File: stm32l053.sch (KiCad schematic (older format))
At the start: 17 parts, among them P1 SWD, P2 CONN_01X23, P3 CONN_01X23, P4 BOOT0, P5 Ext Xtal, SW1 SW_PUSH, U1 STM32_LQFP64

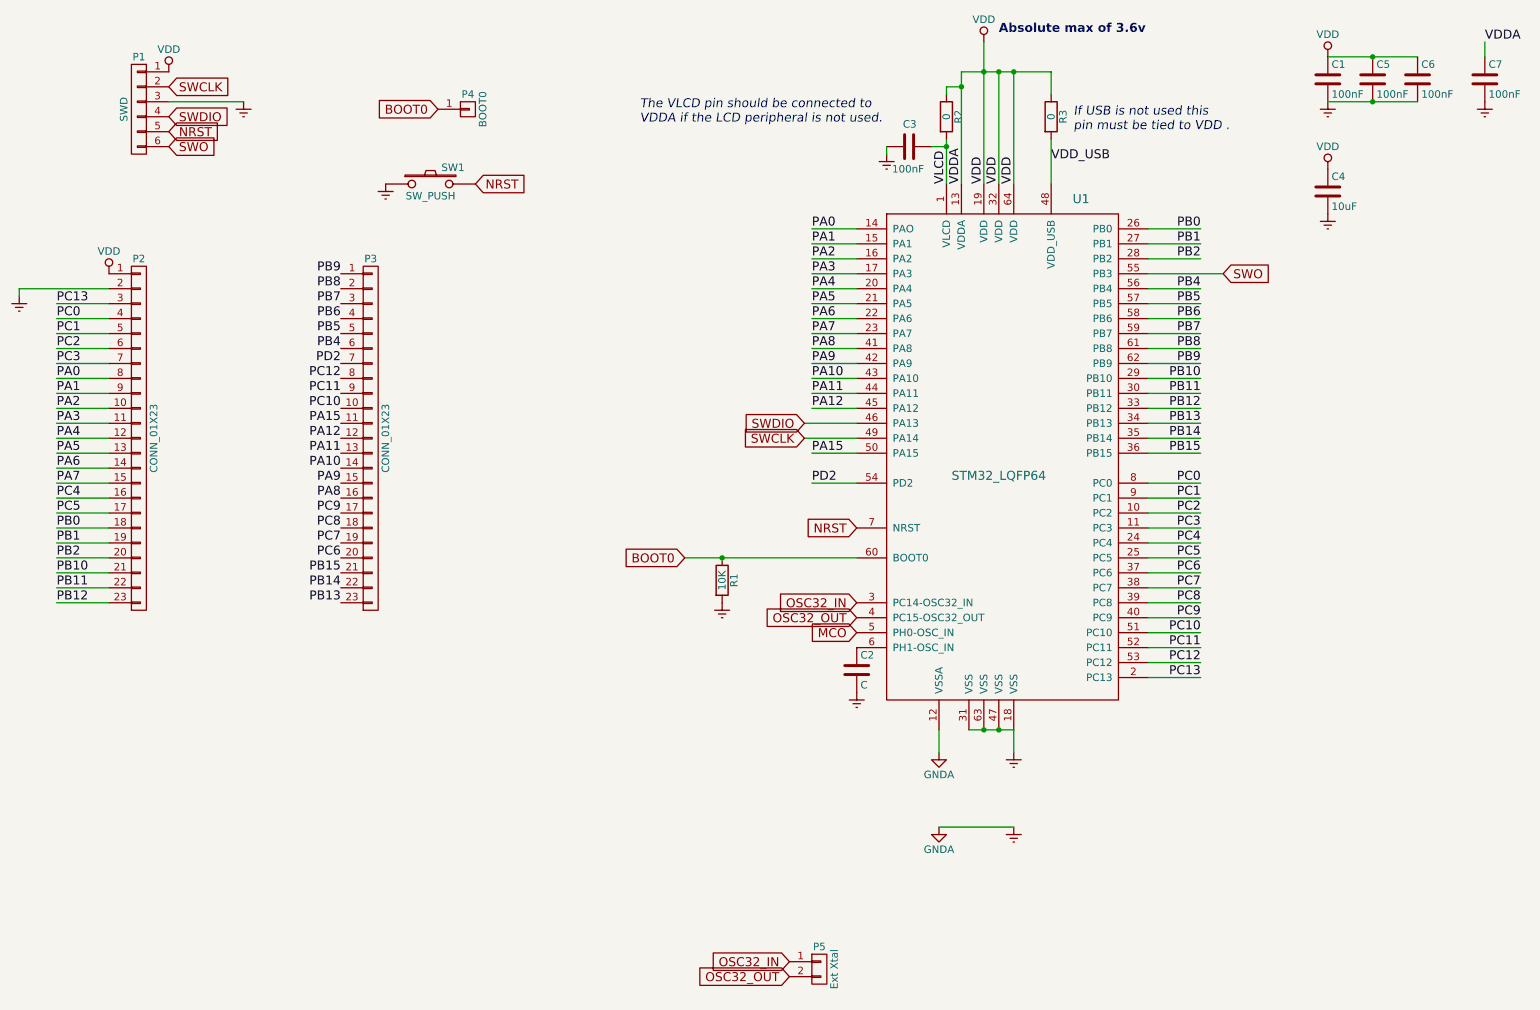
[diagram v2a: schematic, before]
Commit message: GPIO initial routing
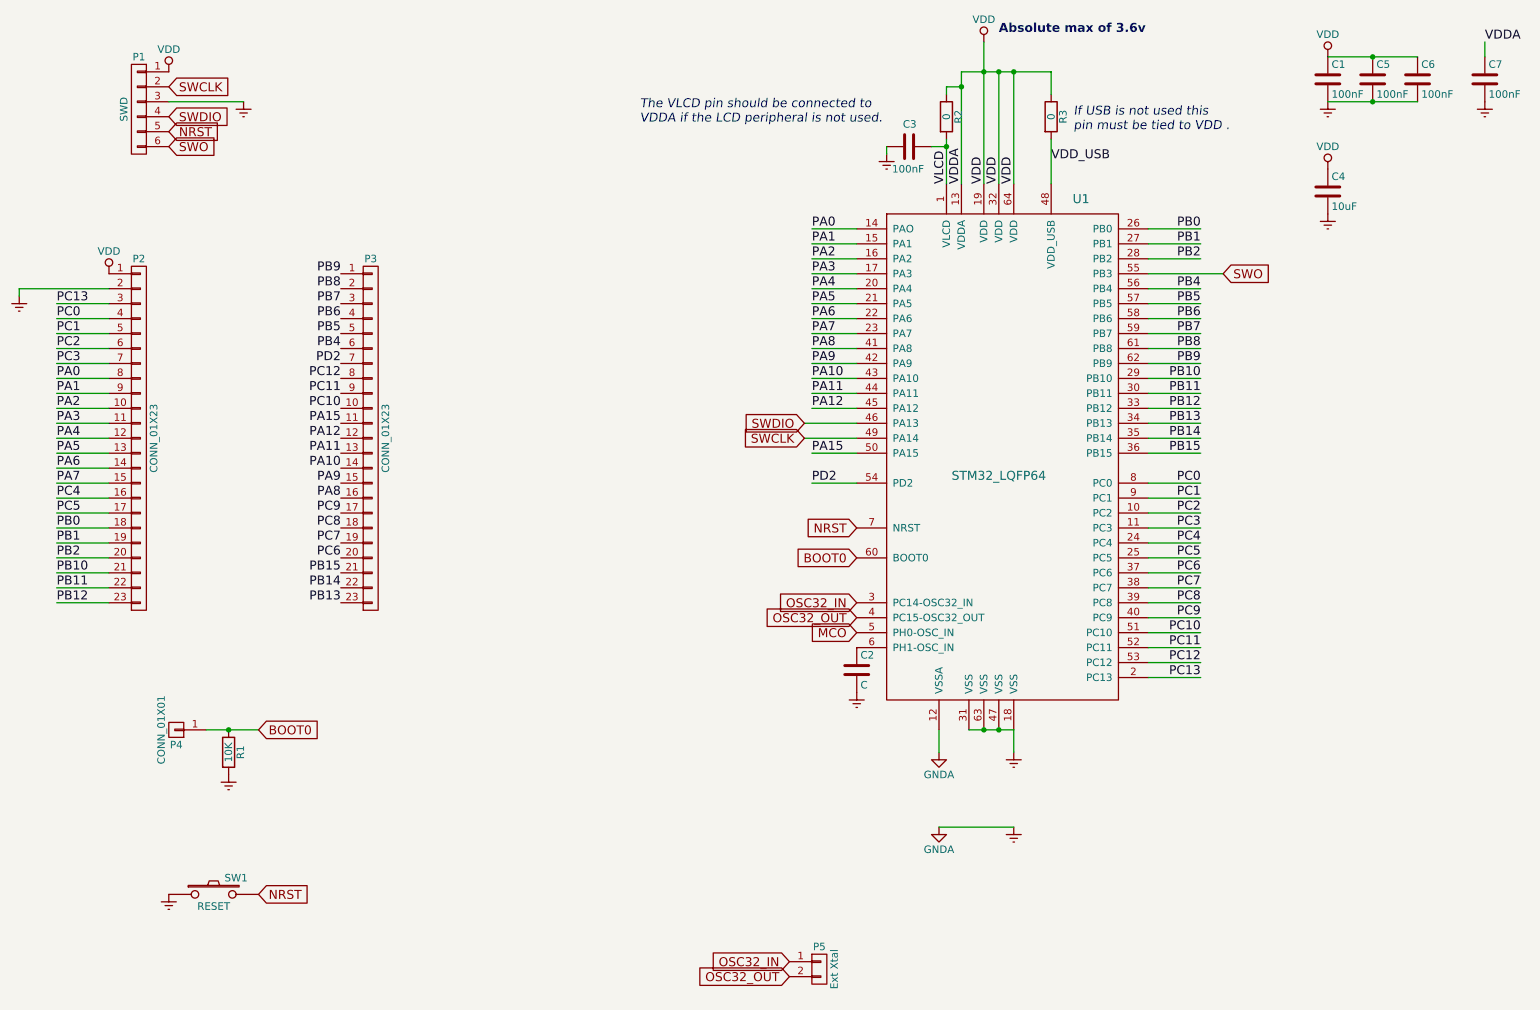
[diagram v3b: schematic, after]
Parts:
- P4: value BOOT0 -> CONN_01X01; footprint Pin_Headers:Pin_Header_Straight_1x01 -> Measurement_Points:Measurement_Point_Round-SMD-Pad_Small
- SW1: value SW_PUSH -> RESET; footprint Buttons_Switches_SMD:SW_SPST_B3U-1000P -> Buttons_Switches_ThroughHole:SW_PUSH_6mm
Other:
- moved on the sheet: R1, SW1
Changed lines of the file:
@@
 L Earth #PWR08
 U 1 1 5802320E
-P 5600 4700
-F 0 "#PWR08" H 5600 4450 50  0001 C CNN
-F 1 "Earth" H 5600 4550 50  0001 C CNN
-F 2 "" H 5600 4700 50  0000 C CNN
-F 3 "" H 5600 4700 50  0000 C CNN
-	1    5600 4700
+P 2300 5850
+F 0 "#PWR08" H 2300 5600 50  0001 C CNN
+F 1 "Earth" H 2300 5700 50  0001 C CNN
+F 2 "" H 2300 5850 50  0000 C CNN
+F 3 "" H 2300 5850 50  0000 C CNN
+	1    2300 5850
 	1    0    0    -1
 $EndComp
@@
 L R R1
 U 1 1 58037533
-P 5600 4550
-F 0 "R1" V 5680 4550 50  0000 C CNN
-F 1 "10K" V 5600 4550 50  0000 C CNN
-F 2 "Resistors_SMD:R_0805_HandSoldering" V 5530 4550 50  0001 C CNN
-F 3 "" H 5600 4550 50  0000 C CNN
-	1    5600 4550
-	1    0    0    -1
-$EndComp
-Text GLabel 5350 4400 0    60   Input ~ 0
+P 2300 5700
+F 0 "R1" V 2380 5700 50  0000 C CNN
+F 1 "10K" V 2300 5700 50  0000 C CNN
+F 2 "Resistors_SMD:R_0805_HandSoldering" V 2230 5700 50  0001 C CNN
+F 3 "" H 2300 5700 50  0000 C CNN
+	1    2300 5700
+	1    0    0    -1
+$EndComp
+Text GLabel 6500 4400 0    60   Input ~ 0
 BOOT0
 Text GLabel 6500 4700 0    60   Input ~ 0
@@
 Text Label 3050 4500 2    60   ~ 0
 PB15
-Wire Wire Line
-	5350 4400 6500 4400
-Connection ~ 5600 4400
 Text Label 8800 3900 2    60   ~ 0
 PC0
@@
 	1    0    0    -1
 $EndComp
-Text GLabel 3700 1400 0    60   Input ~ 0
+Text GLabel 2500 5550 2    60   Input ~ 0
 BOOT0
 $Comp
 L SW_PUSH SW1
 U 1 1 5803EFB1
-P 3650 1900
-F 0 "SW1" H 3800 2010 50  0000 C CNN
-F 1 "SW_PUSH" H 3650 1820 50  0000 C CNN
-F 2 "Buttons_Switches_SMD:SW_SPST_B3U-1000P" H 3650 1900 50  0001 C CNN
-F 3 "" H 3650 1900 50  0000 C CNN
-	1    3650 1900
+P 2200 6650
+F 0 "SW1" H 2350 6760 50  0000 C CNN
+F 1 "RESET" H 2200 6570 50  0000 C CNN
+F 2 "Buttons_Switches_ThroughHole:SW_PUSH_6mm" H 2200 6650 50  0001 C CNN
+F 3 "" H 2200 6650 50  0000 C CNN
+	1    2200 6650
 	1    0    0    -1
 $EndComp
@@
 L Earth #PWR014
 U 1 1 5803F003
-P 3350 1900
-F 0 "#PWR014" H 3350 1650 50  0001 C CNN
-F 1 "Earth" H 3350 1750 50  0001 C CNN
-F 2 "" H 3350 1900 50  0000 C CNN
-F 3 "" H 3350 1900 50  0000 C CNN
-	1    3350 1900
-	1    0    0    -1
-$EndComp
-Text GLabel 3950 1900 2    60   Input ~ 0
+P 1900 6650
+F 0 "#PWR014" H 1900 6400 50  0001 C CNN
+F 1 "Earth" H 1900 6500 50  0001 C CNN
+F 2 "" H 1900 6650 50  0000 C CNN
+F 3 "" H 1900 6650 50  0000 C CNN
+	1    1900 6650
+	1    0    0    -1
+$EndComp
+Text GLabel 2500 6650 2    60   Input ~ 0
 NRST
 $Comp
@@
 F 3 "" H 9650 1950 50  0000 C CNN
 	1    9650 1950
-	1    0    0    -1
-$EndComp
-$Comp
-L CONN_01X01 P4
-U 1 1 5803B76E
-P 3900 1400
-F 0 "P4" H 3900 1500 50  0000 C CNN
-F 1 "BOOT0" V 4000 1400 50  0000 C CNN
-F 2 "Pin_Headers:Pin_Header_Straight_1x01" H 3900 1400 50  0001 C CNN
-F 3 "" H 3900 1400 50  0000 C CNN
-	1    3900 1400
 	1    0    0    -1
 $EndComp
@@
 Connection ~ 7450 1150
 Connection ~ 7550 1150
+$Comp
+L CONN_01X01 P4
+U 1 1 580498F7
+P 1950 5550
+F 0 "P4" H 1950 5650 50  0000 C CNN
+F 1 "CONN_01X01" V 2050 5550 50  0000 C CNN
+F 2 "Measurement_Points:Measurement_Point_Round-SMD-Pad_Small" H 1950 5550 50  0001 C CNN
+F 3 "" H 1950 5550 50  0000 C CNN
+	1    1950 5550
+	-1   0    0    1
+$EndComp
+Wire Wire Line
+	2150 5550 2500 5550
+Connection ~ 2300 5550
 $EndSCHEMATC

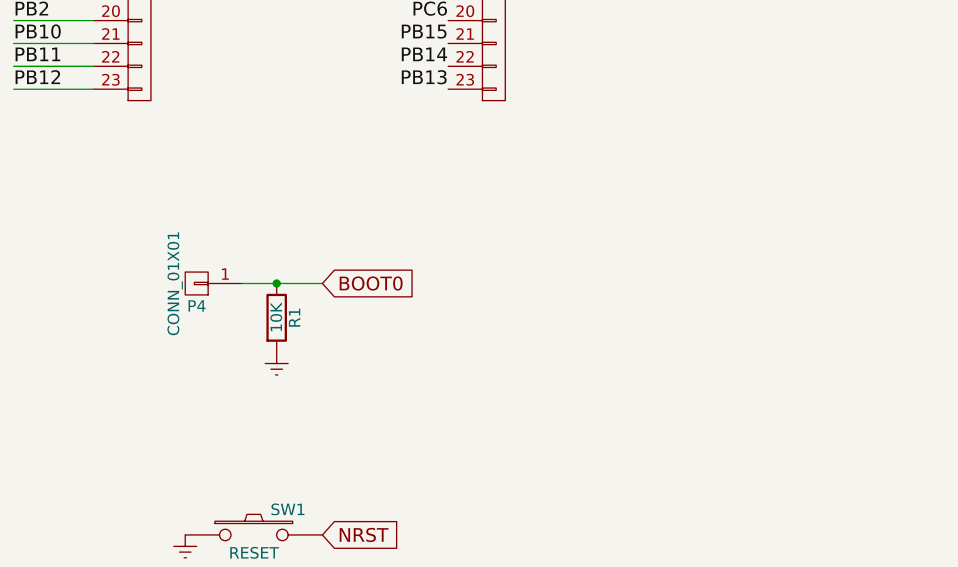
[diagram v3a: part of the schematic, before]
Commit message: SWO header
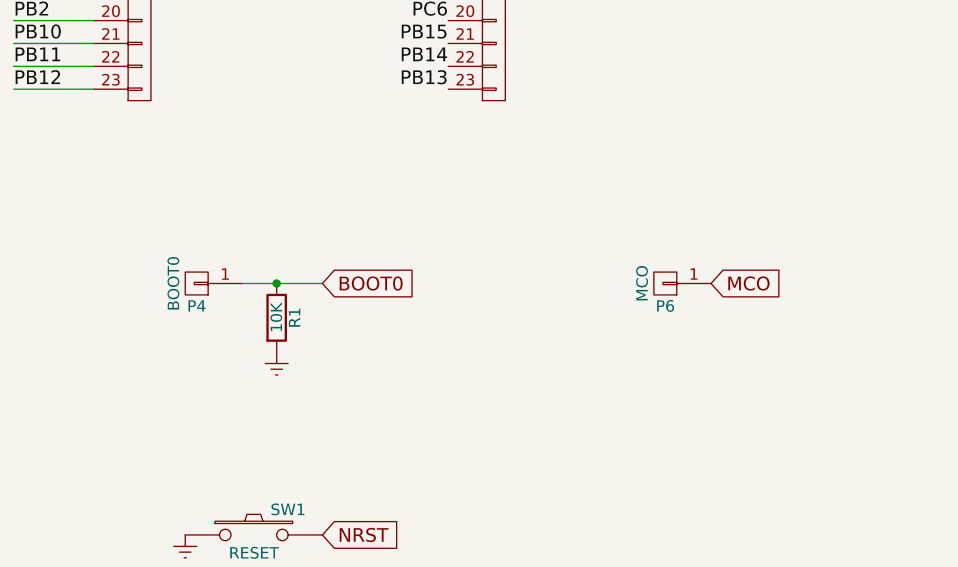
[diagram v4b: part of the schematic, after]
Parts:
- added P6: MCO, Measurement_Points:Measurement_Point_Round-SMD-Pad_Small, symbol CONN_01X01
- P4: value CONN_01X01 -> BOOT0
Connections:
- net MCO: now also P6.1 (P1)
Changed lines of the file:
@@
 $EndComp
 $Comp
-L Earth #PWR01
+L Earth #PWR15
 U 1 1 58021BE1
 P 9650 1350
-F 0 "#PWR01" H 9650 1100 50  0001 C CNN
+F 0 "#PWR15" H 9650 1100 50  0001 C CNN
 F 1 "Earth" H 9650 1200 50  0001 C CNN
 F 2 "" H 9650 1350 50  0000 C CNN
@@
 $EndComp
 $Comp
-L VDD #PWR02
+L VDD #PWR14
 U 1 1 58021C2A
 P 9650 1050
-F 0 "#PWR02" H 9650 900 50  0001 C CNN
+F 0 "#PWR14" H 9650 900 50  0001 C CNN
 F 1 "VDD" H 9650 1200 50  0000 C CNN
 F 2 "" H 9650 1050 50  0000 C CNN
@@
 $EndComp
 $Comp
-L GNDA #PWR03
+L GNDA #PWR10
 U 1 1 58021F75
 P 7050 6200
-F 0 "#PWR03" H 7050 5950 50  0001 C CNN
+F 0 "#PWR10" H 7050 5950 50  0001 C CNN
 F 1 "GNDA" H 7050 6050 50  0000 C CNN
 F 2 "" H 7050 6200 50  0000 C CNN
@@
 $EndComp
 $Comp
-L Earth #PWR04
+L Earth #PWR13
 U 1 1 58021F89
 P 7550 6200
-F 0 "#PWR04" H 7550 5950 50  0001 C CNN
+F 0 "#PWR13" H 7550 5950 50  0001 C CNN
 F 1 "Earth" H 7550 6050 50  0001 C CNN
 F 2 "" H 7550 6200 50  0000 C CNN
@@
 $EndComp
 $Comp
-L GNDA #PWR05
+L GNDA #PWR9
 U 1 1 58022154
 P 7050 5700
-F 0 "#PWR05" H 7050 5450 50  0001 C CNN
+F 0 "#PWR9" H 7050 5450 50  0001 C CNN
 F 1 "GNDA" H 7050 5550 50  0000 C CNN
 F 2 "" H 7050 5700 50  0000 C CNN
@@
 $EndComp
 $Comp
-L Earth #PWR06
+L Earth #PWR12
 U 1 1 580221FA
 P 7550 5700
-F 0 "#PWR06" H 7550 5450 50  0001 C CNN
+F 0 "#PWR12" H 7550 5450 50  0001 C CNN
 F 1 "Earth" H 7550 5550 50  0001 C CNN
 F 2 "" H 7550 5700 50  0000 C CNN
@@
 $EndComp
 $Comp
-L VDD #PWR07
+L VDD #PWR11
 U 1 1 5802295B
 P 7350 950
-F 0 "#PWR07" H 7350 800 50  0001 C CNN
+F 0 "#PWR11" H 7350 800 50  0001 C CNN
 F 1 "VDD" H 7350 1100 50  0000 C CNN
 F 2 "" H 7350 950 50  0000 C CNN
@@
 $EndComp
 $Comp
-L Earth #PWR08
+L Earth #PWR5
 U 1 1 5802320E
 P 2300 5850
-F 0 "#PWR08" H 2300 5600 50  0001 C CNN
+F 0 "#PWR5" H 2300 5600 50  0001 C CNN
 F 1 "Earth" H 2300 5700 50  0001 C CNN
 F 2 "" H 2300 5850 50  0000 C CNN
@@
 $EndComp
 $Comp
-L Earth #PWR09
+L Earth #PWR8
 U 1 1 5803310F
 P 6700 1700
-F 0 "#PWR09" H 6700 1450 50  0001 C CNN
+F 0 "#PWR8" H 6700 1450 50  0001 C CNN
 F 1 "Earth" H 6700 1550 50  0001 C CNN
 F 2 "" H 6700 1700 50  0000 C CNN
@@
 $EndComp
 $Comp
-L Earth #PWR010
+L Earth #PWR7
 U 1 1 58034EA2
 P 6500 5300
-F 0 "#PWR010" H 6500 5050 50  0001 C CNN
+F 0 "#PWR7" H 6500 5050 50  0001 C CNN
 F 1 "Earth" H 6500 5150 50  0001 C CNN
 F 2 "" H 6500 5300 50  0000 C CNN
@@
 $EndComp
 $Comp
-L Earth #PWR011
+L Earth #PWR6
 U 1 1 580369A9
 P 2400 1350
-F 0 "#PWR011" H 2400 1100 50  0001 C CNN
+F 0 "#PWR6" H 2400 1100 50  0001 C CNN
 F 1 "Earth" H 2400 1200 50  0001 C CNN
 F 2 "" H 2400 1350 50  0000 C CNN
@@
 SWO
 $Comp
-L VDD #PWR012
+L VDD #PWR3
 U 1 1 5803734F
 P 1900 1150
-F 0 "#PWR012" H 1900 1000 50  0001 C CNN
+F 0 "#PWR3" H 1900 1000 50  0001 C CNN
 F 1 "VDD" H 1900 1300 50  0000 C CNN
 F 2 "" H 1900 1150 50  0000 C CNN
@@
 PD2
 $Comp
-L VDD #PWR013
+L VDD #PWR2
 U 1 1 5803DE79
 P 1500 2500
-F 0 "#PWR013" H 1500 2350 50  0001 C CNN
+F 0 "#PWR2" H 1500 2350 50  0001 C CNN
 F 1 "VDD" H 1500 2650 50  0000 C CNN
 F 2 "" H 1500 2500 50  0000 C CNN
@@
 $EndComp
 $Comp
-L Earth #PWR014
+L Earth #PWR4
 U 1 1 5803F003
 P 1900 6650
-F 0 "#PWR014" H 1900 6400 50  0001 C CNN
+F 0 "#PWR4" H 1900 6400 50  0001 C CNN
 F 1 "Earth" H 1900 6500 50  0001 C CNN
 F 2 "" H 1900 6650 50  0000 C CNN
@@
 NRST
 $Comp
-L Earth #PWR015
+L Earth #PWR17
 U 1 1 58039244
 P 9650 2100
-F 0 "#PWR015" H 9650 1850 50  0001 C CNN
+F 0 "#PWR17" H 9650 1850 50  0001 C CNN
 F 1 "Earth" H 9650 1950 50  0001 C CNN
 F 2 "" H 9650 2100 50  0000 C CNN
@@
 $EndComp
 $Comp
-L VDD #PWR016
+L VDD #PWR16
 U 1 1 5803924A
 P 9650 1800
-F 0 "#PWR016" H 9650 1650 50  0001 C CNN
+F 0 "#PWR16" H 9650 1650 50  0001 C CNN
 F 1 "VDD" H 9650 1950 50  0000 C CNN
 F 2 "" H 9650 1800 50  0000 C CNN
@@
 Connection ~ 9950 1350
 $Comp
-L Earth #PWR017
+L Earth #PWR18
 U 1 1 5803BDC8
 P 10700 1350
-F 0 "#PWR017" H 10700 1100 50  0001 C CNN
+F 0 "#PWR18" H 10700 1100 50  0001 C CNN
 F 1 "Earth" H 10700 1200 50  0001 C CNN
 F 2 "" H 10700 1350 50  0000 C CNN
@@
 	900  2600 1500 2600
 $Comp
-L Earth #PWR018
+L Earth #PWR1
 U 1 1 5803D0EB
 P 900 2650
-F 0 "#PWR018" H 900 2400 50  0001 C CNN
+F 0 "#PWR1" H 900 2400 50  0001 C CNN
 F 1 "Earth" H 900 2500 50  0001 C CNN
 F 2 "" H 900 2650 50  0000 C CNN
@@
 P 1950 5550
 F 0 "P4" H 1950 5650 50  0000 C CNN
-F 1 "CONN_01X01" V 2050 5550 50  0000 C CNN
+F 1 "BOOT0" V 2050 5550 50  0000 C CNN
 F 2 "Measurement_Points:Measurement_Point_Round-SMD-Pad_Small" H 1950 5550 50  0001 C CNN
 F 3 "" H 1950 5550 50  0000 C CNN
@@
 	2150 5550 2500 5550
 Connection ~ 2300 5550
+Text GLabel 4200 5550 2    60   Input ~ 0
+MCO
+$Comp
+L CONN_01X01 P6
+U 1 1 5804A799
+P 4000 5550
+F 0 "P6" H 4000 5650 50  0000 C CNN
+F 1 "MCO" V 4100 5550 50  0000 C CNN
+F 2 "Measurement_Points:Measurement_Point_Round-SMD-Pad_Small" H 4000 5550 50  0001 C CNN
+F 3 "" H 4000 5550 50  0000 C CNN
+	1    4000 5550
+	-1   0    0    1
+$EndComp
 $EndSCHEMATC
